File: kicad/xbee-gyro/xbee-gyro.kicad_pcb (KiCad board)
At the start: 2 copper layers, 69.2 x 61.6 mm, 18 parts, among them J1 IMU_in, J2 IMU, J3 XBee, SW1 Reset, U1 XBEE-S2C, U2 XC6216D_SOT89

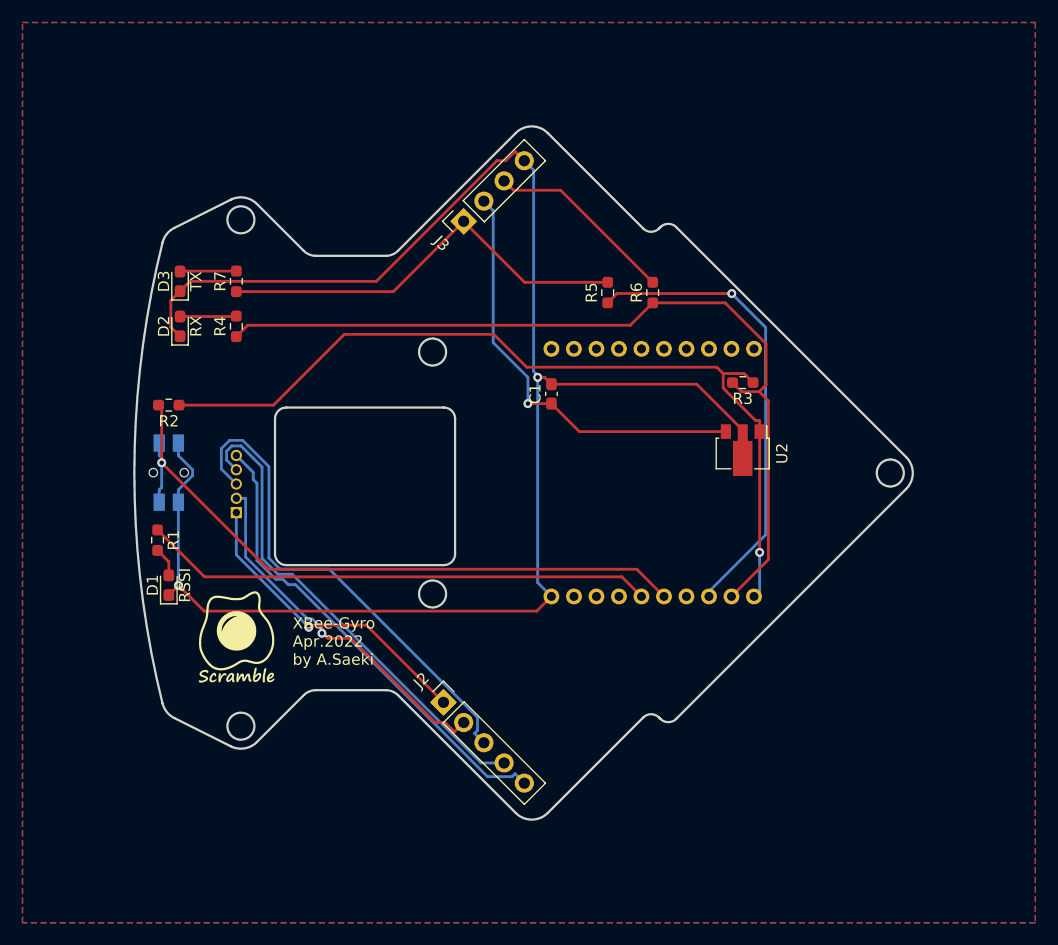
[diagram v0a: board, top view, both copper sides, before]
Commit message: IMU and Xbee board change
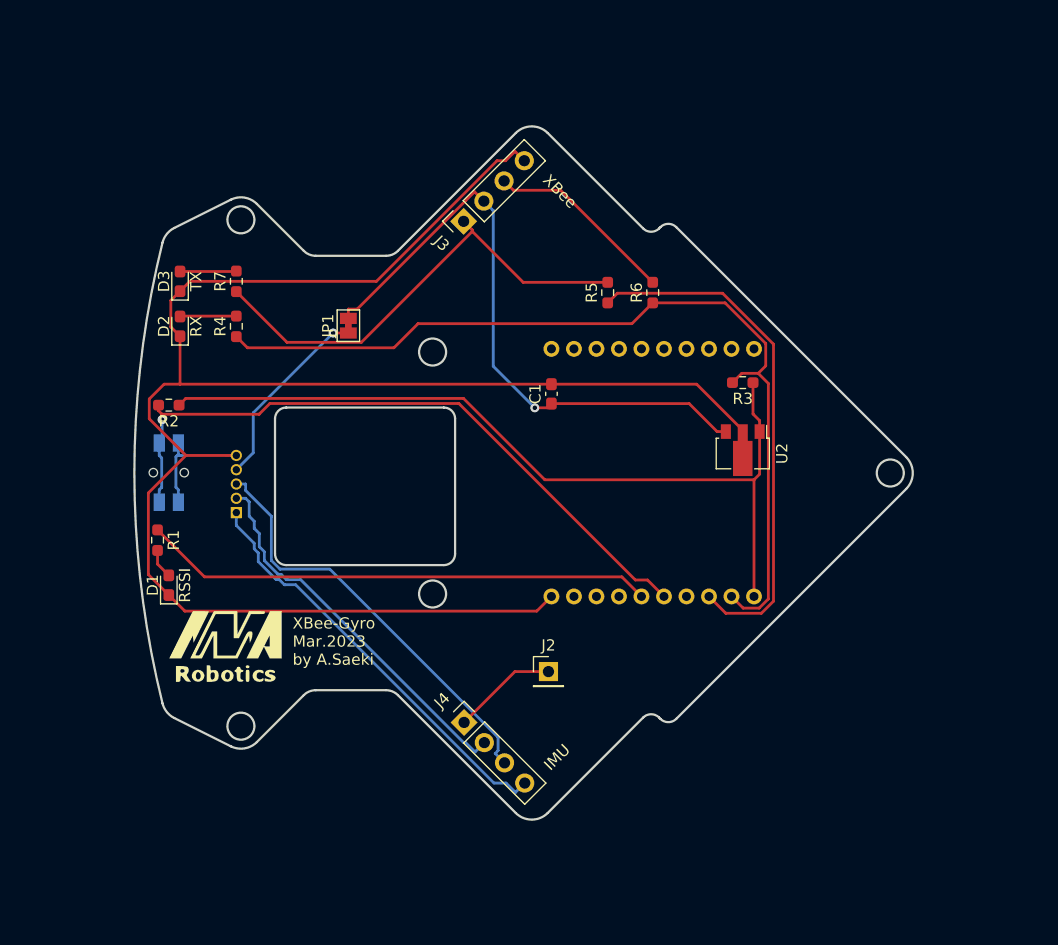
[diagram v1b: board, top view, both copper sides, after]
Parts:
- removed the G*** at (54.0, 130.0)
- added G***: LOGO, 0.main.robot:MMA_Logo, F.Cu at (53.0, 130.6)
- added J4: IMU, Connector_PinSocket_2.54mm:PinSocket_1x04_P2.54mm_Vertical, F.Cu at (74.2, 137.2)
- added JP1: Jumper_2_Bridged, Jumper:SolderJumper-2_P1.3mm_Bridged_Pad1.0x1.5mm, F.Cu at (64.0, 101.9)
- J2: value IMU -> N.C.; footprint Connector_PinSocket_2.54mm:PinSocket_1x05_P2.54mm_Vertical -> Connector_PinHeader_2.54mm:PinHeader_1x01_P2.54mm_Vertical
- moved J2 9.72 mm to (81.7, 132.7), turned to 0 degrees
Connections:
- J1 pad 5: Net-(J1-Pad5) -> GND
- J2 pad 1: Net-(J1-Pad1) -> Net-(J2-Pad1)
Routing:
- net Net-(J1-Pad5): track 42.3 -> 0.00 mm
- net Net-(J1-Pad4): track 43.3 -> 17.1 mm, vias 0 -> 1
- net GND: track 150.4 -> 171.4 mm, vias 2 -> 0
- net +5V: track 38.2 -> 55.9 mm
- net Net-(J1-Pad1): track 27.7 -> 37.7 mm, vias 1 -> 0
- net Net-(J2-Pad1): track 0.00 -> 9.37 mm
- net Net-(J1-Pad3): track 44.4 -> 37.9 mm
- net Net-(R5-Pad1): track 41.6 -> 46.6 mm, vias 1 -> 0
- net Net-(J3-Pad1): track 37.8 -> 42.0 mm
- net Net-(R3-Pad2): track 76.9 -> 80.6 mm
- net Net-(R2-Pad1): track 76.9 -> 73.8 mm, vias 1 -> 0
- net Net-(J1-Pad2): track 32.4 -> 34.0 mm, vias 1 -> 0
- net Net-(R2-Pad2): track 60.2 -> 61.2 mm
- removed copper zone on B.Cu, net GND
- removed copper zone on F.Cu, net GND
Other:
- board text added: "XBee-Gyro Mar.2023 by A.Saeki"
- board text removed: "XBee-Gyro Apr.2022 by A.Saeki"
